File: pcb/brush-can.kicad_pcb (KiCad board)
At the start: 2 copper layers, 57 parts, among them J1 Conn_ARM_SWD_TagConnect_TC203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, J2 Conn_01x04_MountingPin, J3 Conn_01x04_MountingPin, J4 Conn_01x06_MountingPin, J5 Conn_01x06_MountingPin, J6 Conn_01x06_MountingPin, U1 AP62150Z6, U2 NCP176, U3 STM32G431CBUx, U4 TJA1044GTK/3, U5 DRV8876, U6 DRV8876, U7 DRV8876, Y1 16MHz

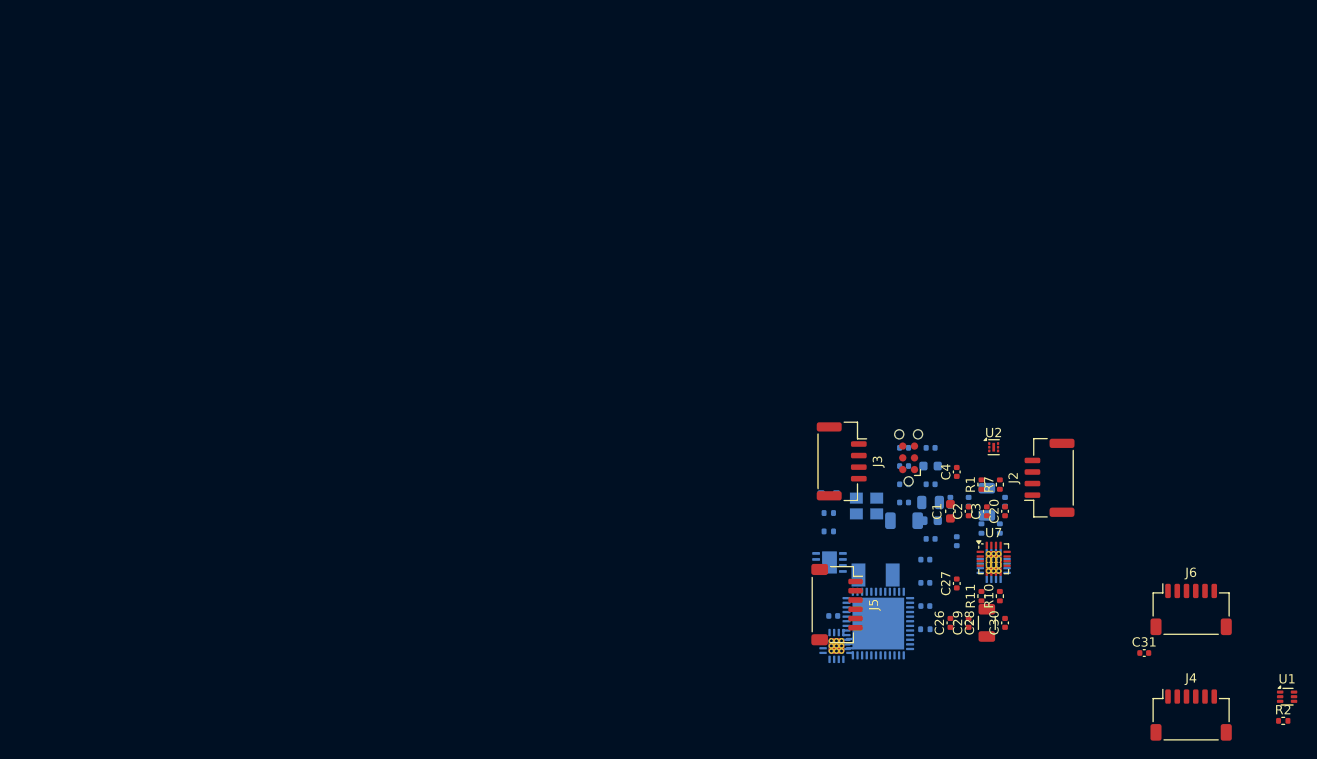
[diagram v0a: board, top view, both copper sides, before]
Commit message: Rough layout of pcb
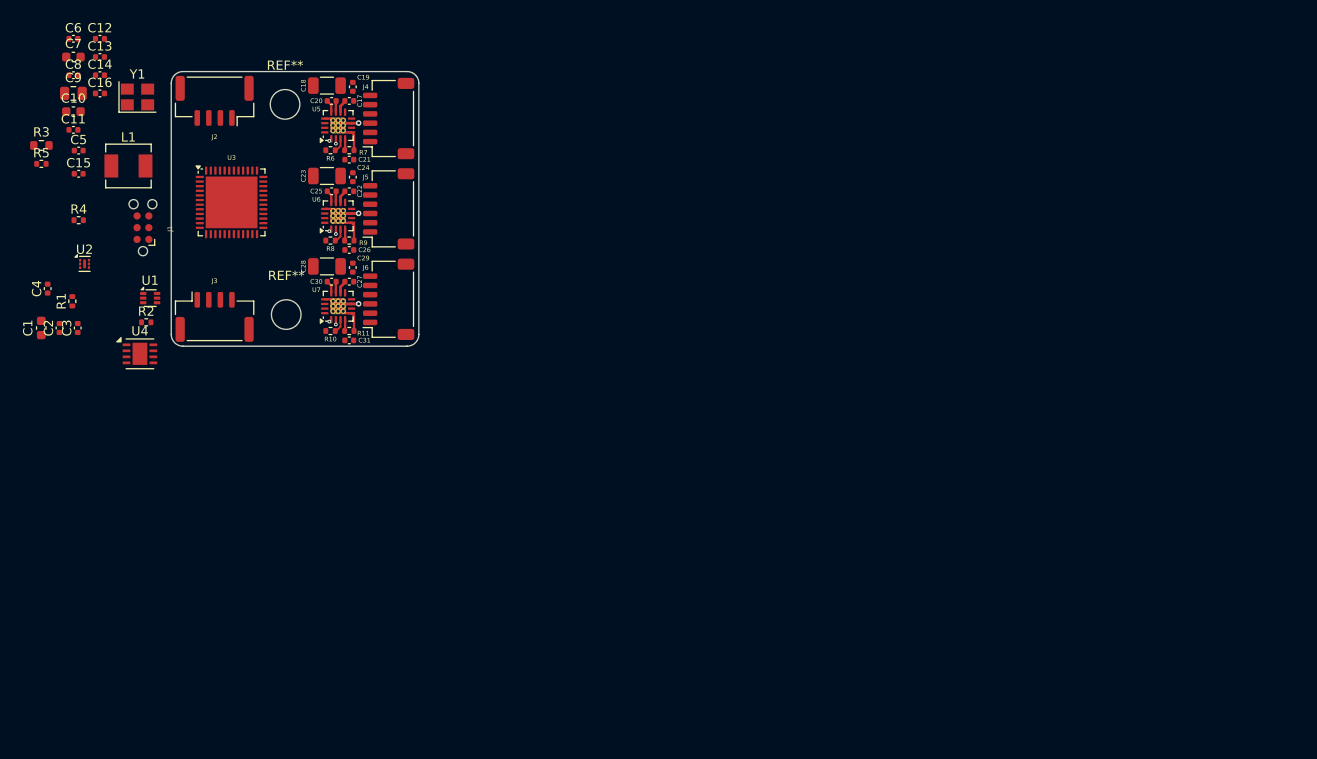
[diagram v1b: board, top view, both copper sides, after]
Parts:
- added REF**: MountingHole_3.2mm_M3, MountingHole:MountingHole_3.2mm_M3, F.Cu at (108.7, 62.2)
- added REF**: MountingHole_3.2mm_M3, MountingHole:MountingHole_3.2mm_M3, F.Cu at (108.6, 39.5)
- C10, C11, C12, C13, C14, C15, C16, C17, C18, C19, C21, C22, C23, C24, C25, C5, C6, C7, C8, C9, L1, R3, R4, R5, R6, R8, R9, U3, U4, U5, U6, Y1: moved to F.Cu
- moved R2 130.3 mm to (93.6, 63.1)
- moved U1 130.3 mm to (94.0, 60.5)
- moved J4 108.1 mm to (119.8, 41.0), turned to 90 degrees
- moved C10 102.7 mm to (85.7, 40.3), turned to 0 degrees
- moved C11 102.7 mm to (85.7, 42.3), turned to 0 degrees
- moved C6 102.7 mm to (85.7, 32.4), turned to 0 degrees
- moved C7 102.7 mm to (85.7, 34.4), turned to 0 degrees
- moved C8 102.7 mm to (85.7, 36.3), turned to 0 degrees
- moved C9 102.7 mm to (85.7, 38.3), turned to 0 degrees
- moved C15 101.7 mm to (86.3, 47.0), turned to 0 degrees
- moved C5 101.7 mm to (86.3, 44.5), turned to 0 degrees
- moved R4 101.7 mm to (86.3, 52.0), turned to 0 degrees
- moved C3 100.3 mm to (86.2, 63.7)
- moved C4 100.3 mm to (82.9, 59.4)
- moved R1 100.3 mm to (85.6, 60.8)
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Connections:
- net Net-(J4-Pin_1) renamed /Driver1/OUT1
- net Net-(J4-Pin_2) renamed /Driver1/OUT2
- net Net-(J5-Pin_1) renamed /Driver2/OUT1
- net Net-(J5-Pin_2) renamed /Driver2/OUT2
- net Net-(J6-Pin_1) renamed /Driver3/OUT1
- net Net-(J6-Pin_2) renamed /Driver3/OUT2
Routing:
- net GND: track 0.00 -> 17.3 mm, vias 0 -> 3
- net /PMS3: track 0.00 -> 1.53 mm
- net /PMS1: track 0.00 -> 1.53 mm
- net /PMS2: track 0.00 -> 1.53 mm
- net Net-(U7-VCP): track 0.00 -> 1.40 mm
- net Net-(U5-VCP): track 0.00 -> 1.40 mm
- net Net-(U6-VCP): track 0.00 -> 1.40 mm
- net Net-(U7-CPL): track 0.00 -> 1.39 mm
- net Net-(U5-CPL): track 0.00 -> 1.39 mm
- net Net-(U6-CPL): track 0.00 -> 1.39 mm
- net /IPR1: track 0.00 -> 1.25 mm
- net /IPR3: track 0.00 -> 1.25 mm
- net /IPR2: track 0.00 -> 1.25 mm
- net Net-(U7-CPH): track 0.00 -> 1.22 mm
- net Net-(U5-CPH): track 0.00 -> 1.22 mm
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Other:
- board outline added: 26.8 x 29.7 mm

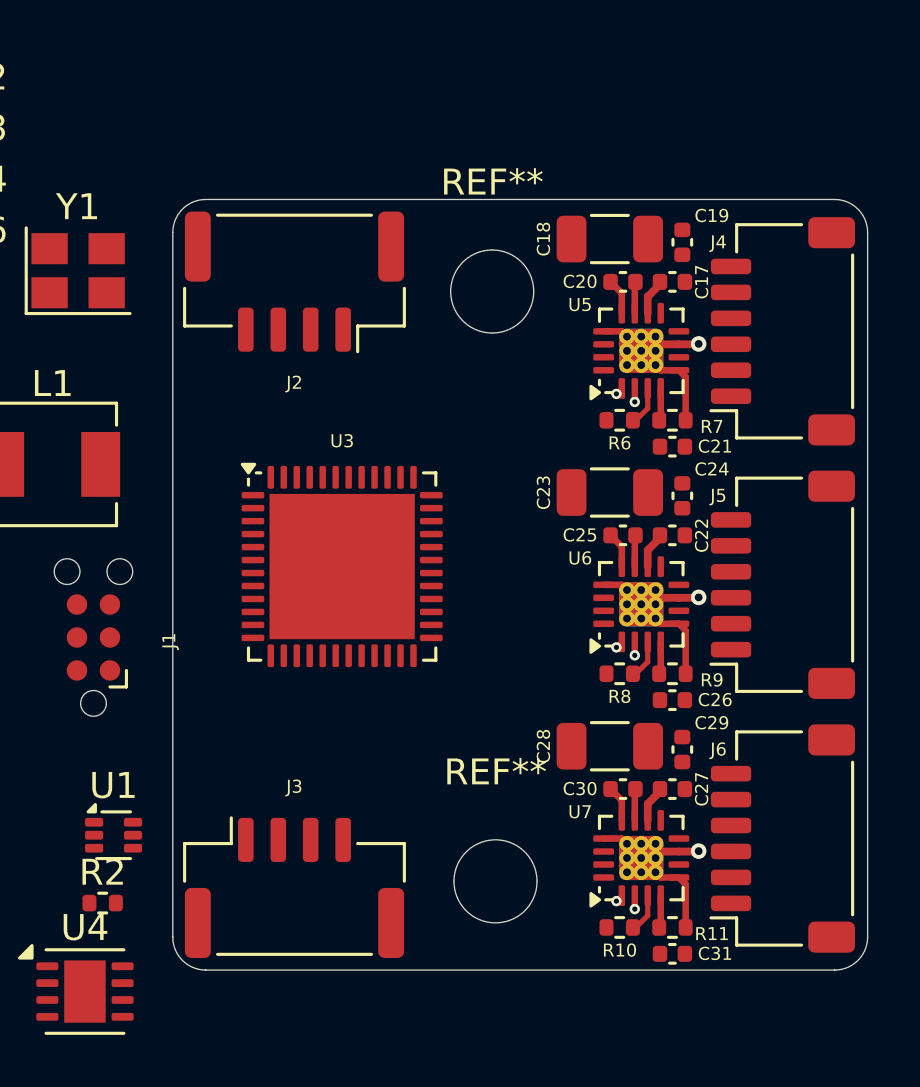
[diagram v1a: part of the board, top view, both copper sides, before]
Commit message: Add inserts and change CAN connection
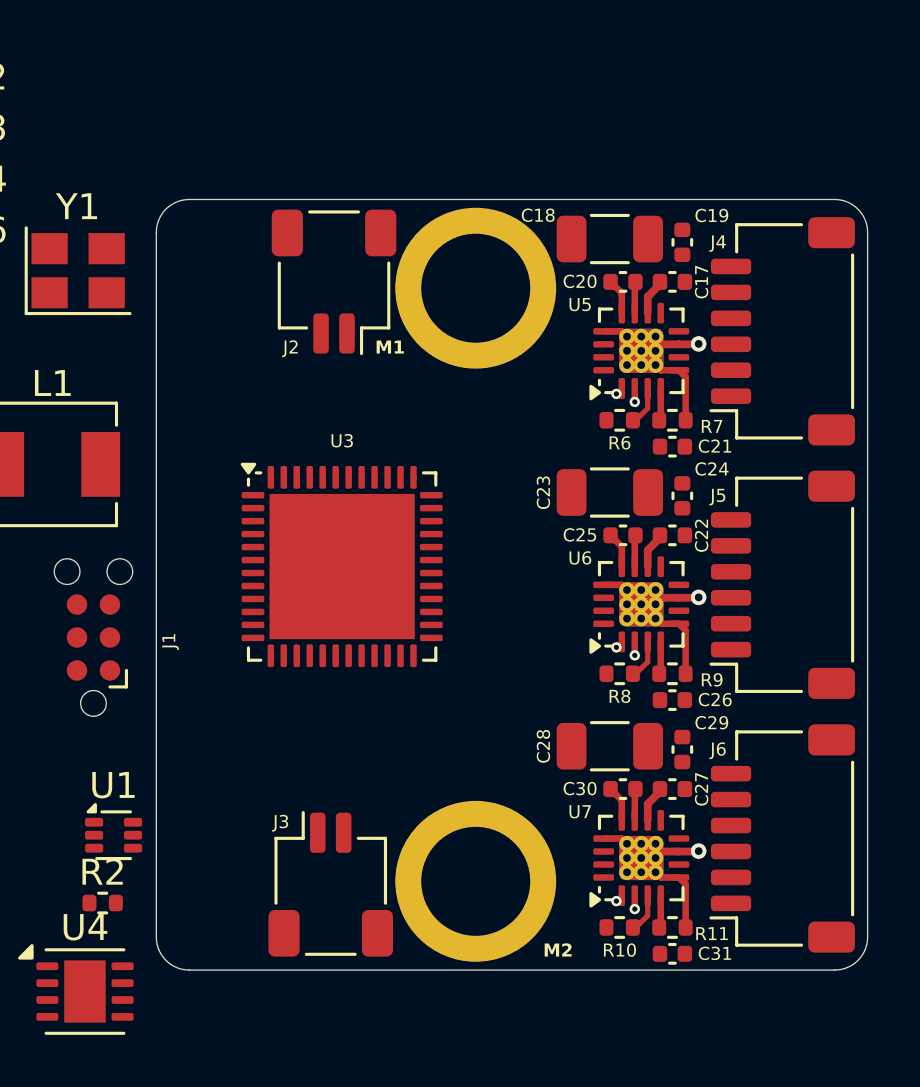
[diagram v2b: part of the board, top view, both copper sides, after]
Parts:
- removed REF** (x2): MountingHole_3.2mm_M3, MountingHole:MountingHole_3.2mm_M3
- added M1: 24939, User_Footprints:24939, F.Cu at (108.0, 39.4)
- added M2: 24939, User_Footprints:24939, F.Cu at (108.0, 62.2)
- J2, J3: value Conn_01x04_MountingPin -> Conn_01x02_MountingPin; footprint Connector_JST:JST_GH_SM04B-GHS-TB_1x04-1MP_P1.25mm_Horizontal -> Connector_JST:JST_SH_SM02B-SRSS-TB_1x02-1MP_P1.00mm_Horizontal
- moved J2 1.52 mm to (102.5, 39.1)
- moved J3 1.40 mm to (102.4, 62.4)
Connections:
- J2 pad 1: +12V -> /CANL
- J2 pad 2: /CANL -> /CANH
- J3 pad 1: +12V -> /CANL
- J3 pad 2: /CANL -> /CANH
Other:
- board size 26.8 x 29.7 mm -> 27.4 x 29.7 mm

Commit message: Finish layout
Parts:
- removed C2: 100n, Capacitor_SMD:C_0402_1005Metric
- added J7: Conn_01x02_Pin, User_Footprints:PowerPins, F.Cu at (97.6, 64.1)
- added J8: Conn_01x02_Pin, User_Footprints:PowerPins, F.Cu at (97.5, 37.5)
- C1: footprint Capacitor_SMD:C_0603_1608Metric -> Capacitor_SMD:C_0402_1005Metric
- J1: moved to B.Cu
- L1: footprint Inductor_SMD:L_Sunlord_MWSA0412S -> Inductor_SMD:L_Chilisin_BMRA00040420
- moved C3 28.3 mm to (110.7, 49.5)
- moved C6 26.4 mm to (101.0, 53.8), turned to -90 degrees
- moved C4 25.8 mm to (108.7, 57.6), turned to 0 degrees
- moved C15 25.4 mm to (111.5, 44.2), turned to 90 degrees
- moved R4 24.9 mm to (111.2, 51.1)
- moved C14 24.9 mm to (97.7, 59.5)
- moved C13 24.3 mm to (99.9, 55.9), turned to -90 degrees
- moved R5 24.0 mm to (106.2, 47.6), turned to -90 degrees
- moved C12 22.5 mm to (105.2, 47.6), turned to 90 degrees
- moved R1 21.1 mm to (97.3, 43.2), turned to -90 degrees
- moved C16 21.1 mm to (107.7, 47.1), turned to 180 degrees
- moved C1 20.2 mm to (99.9, 53.9), turned to -90 degrees
- moved R2 20.1 mm to (96.3, 43.2), turned to 90 degrees
- moved C5 18.6 mm to (101.0, 55.9), turned to -90 degrees
- moved R3 18.0 mm to (97.3, 53.8), turned to 180 degrees
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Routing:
- net /FLT3: track 0.52 -> 1.11 mm, vias 1 -> 2

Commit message: Wire most power
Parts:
- moved C16 3.42 mm to (105.9, 44.2), turned to -90 degrees
- moved J7 2.79 mm to (97.5, 61.3), turned to 0 degrees
- moved J8 2.79 mm to (97.5, 40.3), turned to 180 degrees
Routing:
- net GND: track 17.3 -> 155.5 mm, vias 3 -> 38
- net +3V3: track 0.00 -> 67.9 mm, vias 0 -> 6
- net /CANH: track 0.00 -> 32.9 mm, vias 0 -> 4
- net /CANL: track 0.00 -> 32.5 mm, vias 0 -> 3
- net +5V: track 0.00 -> 31.4 mm, vias 0 -> 3
- net /CNTX: track 0.00 -> 17.8 mm, vias 0 -> 2
- net +12V: track 0.00 -> 15.2 mm, vias 0 -> 2
- net /CNRX: track 0.00 -> 13.6 mm
- net /SWO: track 0.00 -> 12.5 mm, vias 0 -> 1
- net /XTALI: track 0.00 -> 9.63 mm
- net /RST: track 0.00 -> 8.96 mm
- net /SW: track 0.00 -> 8.35 mm
- net /SWCLK: track 0.00 -> 7.88 mm, vias 0 -> 1
- net /SWDIO: track 0.00 -> 5.73 mm, vias 0 -> 1
- net /XTALR: track 0.00 -> 4.51 mm
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- added copper zone on In2.Cu, net +12V
- added copper zone on In1.Cu, net GND
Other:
- copper layers 2 -> 4

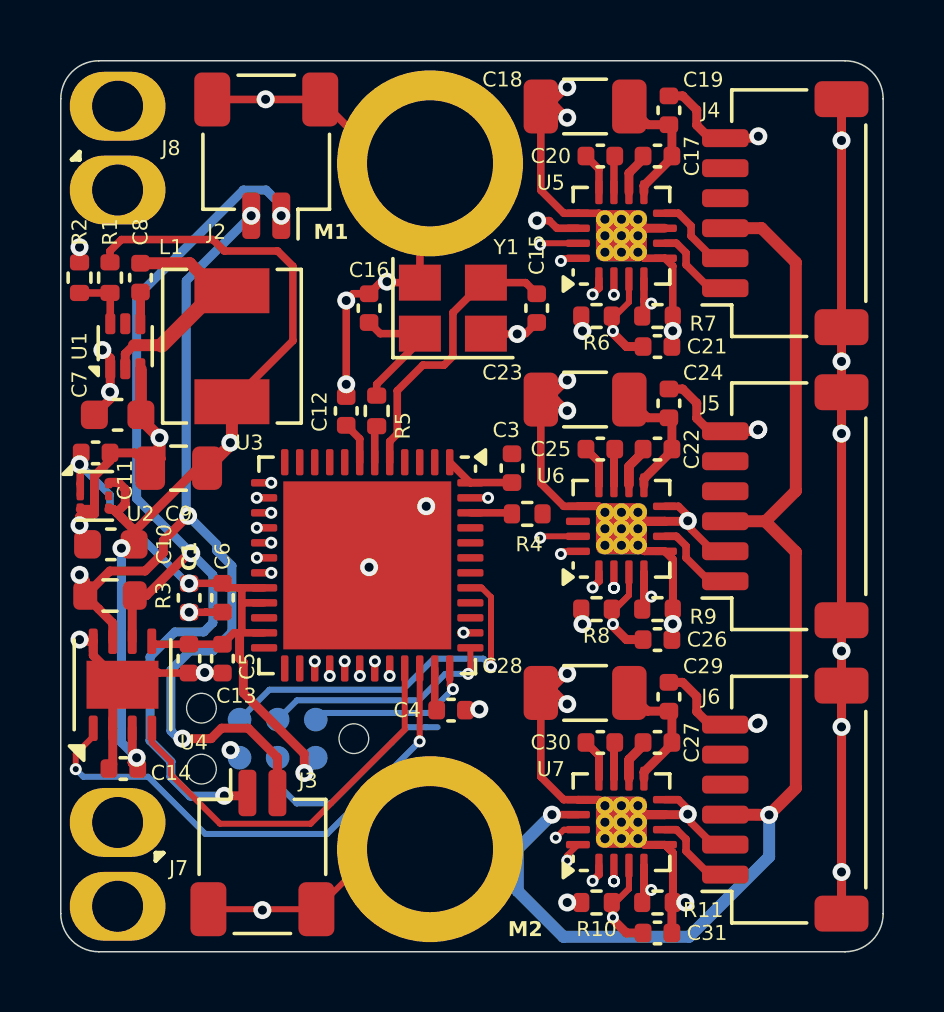
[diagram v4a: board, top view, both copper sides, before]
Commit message: Finish routing and rule checking
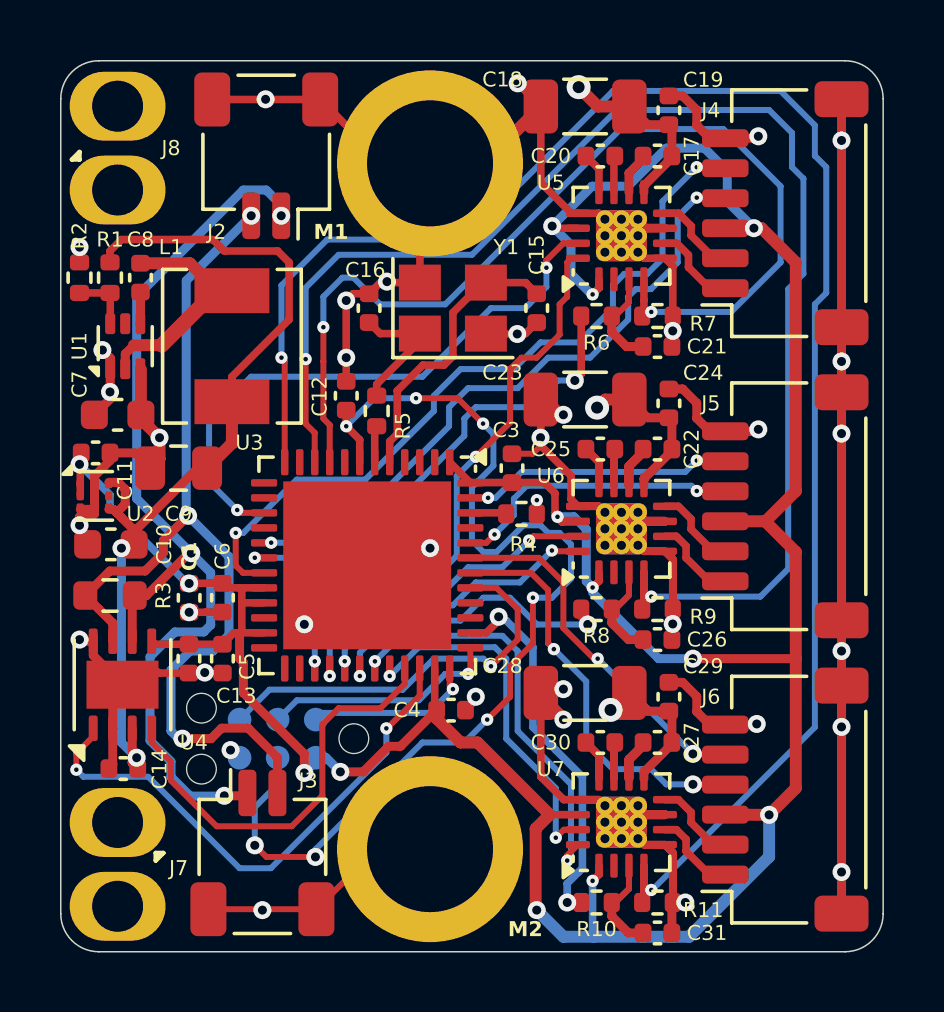
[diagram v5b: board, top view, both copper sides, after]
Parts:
- C21, C26, C31: value 1u -> 10u
- moved C12 0.51 mm to (105.2, 47.1)
- moved R4 0.19 mm to (111.0, 51.1)
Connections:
- C21 pad 1: /PMS1 -> Net-(U5-VREF)
- C26 pad 1: /PMS2 -> Net-(U6-VREF)
- C31 pad 1: /PMS3 -> Net-(U7-VREF)
- R10 pad 1: /PMS3 -> Net-(U7-VREF)
- R6 pad 1: /PMS1 -> Net-(U5-VREF)
- R8 pad 1: /PMS2 -> Net-(U6-VREF)
- U3 pad 10: /IPR3 -> /IPR2
- U3 pad 11: /ECA1 -> unconnected-(U3-PA3-Pad11)
- U3 pad 12: /ECA2 -> /IPR3
- U3 pad 13: /ECA3 -> unconnected-(U3-PA5-Pad13)
- U3 pad 14: /PMS1 -> unconnected-(U3-PA6-Pad14)
- U3 pad 15: /PMS2 -> /INA1
- U3 pad 16: /PMS3 -> unconnected-(U3-PC4-Pad16)
- U3 pad 17: /ECB1 -> /ECA1
- U3 pad 18: /ECB2 -> /PLM1
- U3 pad 19: /ECB3 -> /ECB1
- U3 pad 2: /SLP3 -> unconnected-(U3-PC13-Pad2)
- U3 pad 28: /INB2 -> /INA2
- U3 pad 29: /INB3 -> /INB2
- U3 pad 3: /FLT2 -> unconnected-(U3-PC14-Pad3)
- U3 pad 30: /INA1 -> /PLM2
- U3 pad 31: /INA2 -> /INB3
- U3 pad 4: /SLP2 -> unconnected-(U3-PC15-Pad4)
- U3 pad 42: /FLT1 -> /ECA3
- U3 pad 43: /SLP1 -> /ECB3
- U3 pad 44: /PLM1 -> /ECA2
- U3 pad 45: /PLM2 -> unconnected-(U3-PB7-Pad45)
- U3 pad 47: /FLT3 -> /ECB2
- U3 pad 8: /IPR1 -> unconnected-(U3-PA0-Pad8)
- U3 pad 9: /IPR2 -> /IPR1
- U5 pad 1: /SLP1 -> +3V3
- U5 pad 2: /FLT1 -> /Driver1/FLT
- U5 pad 3: /PMS1 -> Net-(U5-VREF)
- U6 pad 1: /SLP2 -> +3V3
- U6 pad 2: /FLT2 -> /Driver2/FLT
- U6 pad 3: /PMS2 -> Net-(U6-VREF)
- U7 pad 1: /SLP3 -> +3V3
- U7 pad 2: /FLT3 -> /Driver3/FLT
- U7 pad 3: /PMS3 -> Net-(U7-VREF)
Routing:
- net /IPR3: track 3.11 -> 58.1 mm, vias 1 -> 2
- net /IPR2: track 3.11 -> 47.9 mm, vias 1 -> 2
- net +3V3: track 67.9 -> 107.4 mm, vias 6 -> 13
- net /IPR1: track 1.86 -> 33.8 mm, vias 1 -> 2
- net /RST: track 8.96 -> 36.2 mm, vias 0 -> 7
- net /ECB1: track 0.00 -> 25.4 mm, vias 1 -> 2
- net /ECA1: track 0.00 -> 21.6 mm, vias 0 -> 2
- net /INA1: track 1.28 -> 19.6 mm
- net /INB1: track 0.61 -> 18.6 mm
- net /PLM1: track 0.51 -> 15.7 mm, vias 1 -> 2
- net /ECA3: track 0.00 -> 13.7 mm, vias 1 -> 2
- net /INB3: track 0.68 -> 13.8 mm
- net /PLM3: track 0.47 -> 12.8 mm
- net /ECB3: track 0.00 -> 12.1 mm, vias 1 -> 2
- net /INA3: track 0.85 -> 11.9 mm
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
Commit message: Finish final details
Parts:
- added G1: LOGO, LOGO, B.Cu at (108.5, 49.9)
- R1: value 52k3 -> 56k
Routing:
- net /ECA1: track 21.6 -> 25.3 mm
- net /ECB1: track 25.4 -> 28.8 mm
- net /IPR3: track 58.1 -> 60.5 mm
- net +3V3: track 107.4 -> 108.4 mm
- net GND: track 156.9 -> 157.5 mm, vias 34 -> 45
- net /IPR1: track 33.8 -> 34.2 mm, vias 2 -> 4
- added copper zone on B.Cu, net GND
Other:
- board text added: "12V"
- board text added: "3V3"
- board text added: "A"
- board text added: "B"
- board text added: "CANH"
- board text added: "CANL"
- board text added: "Designed by Miguel Flores-Acton"
- board text added: "GND"
- board text added: "KEEPOUT"
- board text added: "M1"
- board text added: "M2"
- board text added: "M3"
- board text added: "O1"
- board text added: "O2"
